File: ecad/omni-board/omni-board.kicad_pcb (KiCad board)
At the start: 2 copper layers, 6 parts, among them J1 Motor_BTS7960_01, J2 Motor_BTS7960_02, J3 Motor_BTS7960_03, J4 Motor_BTS7960_04, U1 ESP32-S3-Zero, U2 ESP32-S3-DevKitC

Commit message: update for production
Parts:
- added C1: 0.1uF, Capacitor_SMD:C_1206_3216Metric_Pad1.33x1.80mm_HandSolder, F.Cu at (144.8, 79.4)
- added C2: 1uF, Capacitor_SMD:CP_Elec_5x5.4, F.Cu at (149.9, 79.4)
- added C3: 22uF, Capacitor_SMD:CP_Elec_5x5.4, F.Cu at (139.1, 92.2)
- added D1: SS14, Diode_SMD:D_SMA_Handsoldering, F.Cu at (148.0, 73.7)
- added D2: LED_Small, LED_SMD:LED_1206_3216Metric_Pad1.42x1.75mm_HandSolder, F.Cu at (128.3, 106.7)
- added D3: LED_Small, LED_SMD:LED_1206_3216Metric_Pad1.42x1.75mm_HandSolder, F.Cu at (128.3, 100.3)
- added D4: LED_Small, LED_SMD:LED_1206_3216Metric_Pad1.42x1.75mm_HandSolder, F.Cu at (128.3, 103.5)
- added H1: MountingHole_Pad, MountingHole:MountingHole_3.2mm_M3_Pad_Via, F.Cu at (180.0, 75.0)
- added H2: MountingHole_Pad, MountingHole:MountingHole_3.2mm_M3_Pad_Via, F.Cu at (130.0, 125.0)
- added H3: MountingHole_Pad, MountingHole:MountingHole_3.2mm_M3_Pad_Via, F.Cu at (180.0, 125.0)
- added H4: MountingHole_Pad, MountingHole:MountingHole_3.2mm_M3_Pad_Via, F.Cu at (130.0, 75.0)
- added J18: Conn_01x04, Connector_Molex:Molex_KK-254_AE-6410-04A_1x04_P2.54mm_Vertical, F.Cu at (181.0, 100.3)
- added J19: Conn_01x04, Connector_Molex:Molex_KK-254_AE-6410-04A_1x04_P2.54mm_Vertical, F.Cu at (181.0, 88.9)
- added J7: Con Batt, Connector_AMASS:AMASS_XT60-M_1x02_P7.20mm_Vertical, F.Cu at (130.2, 92.3)
- added JP1: SolderJumper_3_Open, Jumper:SolderJumper-3_P2.0mm_Open_TrianglePad1.0x1.5mm, F.Cu at (154.9, 108.6)
- added R1: 10k, Resistor_SMD:R_1206_3216Metric_Pad1.30x1.75mm_HandSolder, F.Cu at (168.3, 94.0)
- added R18: 10k, Resistor_SMD:R_1206_3216Metric_Pad1.30x1.75mm_HandSolder, B.Cu at (178.4, 92.4)
- added R19: 10k, Resistor_SMD:R_1206_3216Metric_Pad1.30x1.75mm_HandSolder, B.Cu at (175.9, 92.4)
- added R2: 1k, Resistor_SMD:R_1206_3216Metric_Pad1.30x1.75mm_HandSolder, F.Cu at (134.0, 100.3)
- added R21: 1k, Resistor_SMD:R_1206_3216Metric_Pad1.30x1.75mm_HandSolder, F.Cu at (134.0, 106.7)
- added R22: 1k, Resistor_SMD:R_1206_3216Metric_Pad1.30x1.75mm_HandSolder, F.Cu at (134.0, 103.5)
- U2: value ESP32-S3-DevKitC -> R-78E5.0-1.0; footprint PCM_Espressif:ESP32-S3-DevKitC -> Converter_DCDC:Converter_DCDC_RECOM_R-78E-0.5_THT
- moved J4 41.0 mm to (170.1, 116.2)
- moved J3 40.8 mm to (159.3, 116.2)
- moved J2 40.7 mm to (148.5, 116.2)
- moved J1 40.6 mm to (137.7, 116.2)
- moved U2 37.9 mm to (145.7, 88.4), turned to -90 degrees
- moved U1 28.1 mm to (165.0, 83.8)
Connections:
- U1 pad 1: unconnected-(U1-5V-Pad1) -> Net-(D1-K)
- U1 pad 10: L_PWM_03 -> EN_MOTORS
- U1 pad 13: R_PWM_04 -> L_PWM_04
- U1 pad 14: L_PWM_04 -> R_PWM_04
- U1 pad 15: EN_MOTORS -> L_PWM_03
- U2 pad 1: Net-(U2-3V3-Pad1) -> +12V
- U2 pad 2: Net-(U2-3V3-Pad1) -> GND
- U2 pad 3: unconnected-(U2-CHIP_PU-Pad3) -> +5V
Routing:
- net +3.3V: track 0.00 -> 120.4 mm, vias 0 -> 2
- net EN_MOTORS: track 0.00 -> 67.7 mm
- net +5V: track 0.00 -> 66.9 mm
- net VCC: track 0.00 -> 62.1 mm
- net R_PWM_01: track 0.00 -> 48.2 mm
- net L_PWM_01: track 0.00 -> 43.2 mm
- net L_PWM_03: track 0.00 -> 43.1 mm
- net R_PWM_04: track 0.00 -> 36.4 mm
- net L_PWM_04: track 0.00 -> 33.4 mm
- net +12V: track 0.00 -> 33.1 mm
- net R_PWM_02: track 0.00 -> 32.4 mm
- net SCL: track 0.00 -> 30.3 mm
- net L_PWM_02: track 0.00 -> 28.5 mm
- net R_PWM_03: track 0.00 -> 25.9 mm
- net SDA: track 0.00 -> 24.7 mm
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- added copper zone on B.Cu, net GND
- added copper zone on F.Cu, net GND
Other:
- board outline added: 60 x 60 mm

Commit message: sbus connector added
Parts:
- added J5: Conn_01x03, Connector_PinHeader_2.54mm:PinHeader_1x03_P2.54mm_Vertical, F.Cu at (176.5, 83.2)
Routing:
- net +5V: track 66.9 -> 127.7 mm
- net SBUS: track 0.00 -> 8.95 mm

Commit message: update silkscreen
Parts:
- moved U2 0.97 mm to (144.8, 88.4)
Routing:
- net +5V: track 127.7 -> 130.0 mm
- net +12V: track 33.1 -> 32.2 mm
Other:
- board text added: "+"
- board text added: "12V"
- board text added: "3.3V"
- board text added: "5V"
- board text added: "ESP32-S3 ZERO"
- board text added: "I2C"
- board text added: "MOTOR 1"
- board text added: "MOTOR 2"
- board text added: "MOTOR 3"
- board text added: "MOTOR 4"
- board text added: "Sbus"

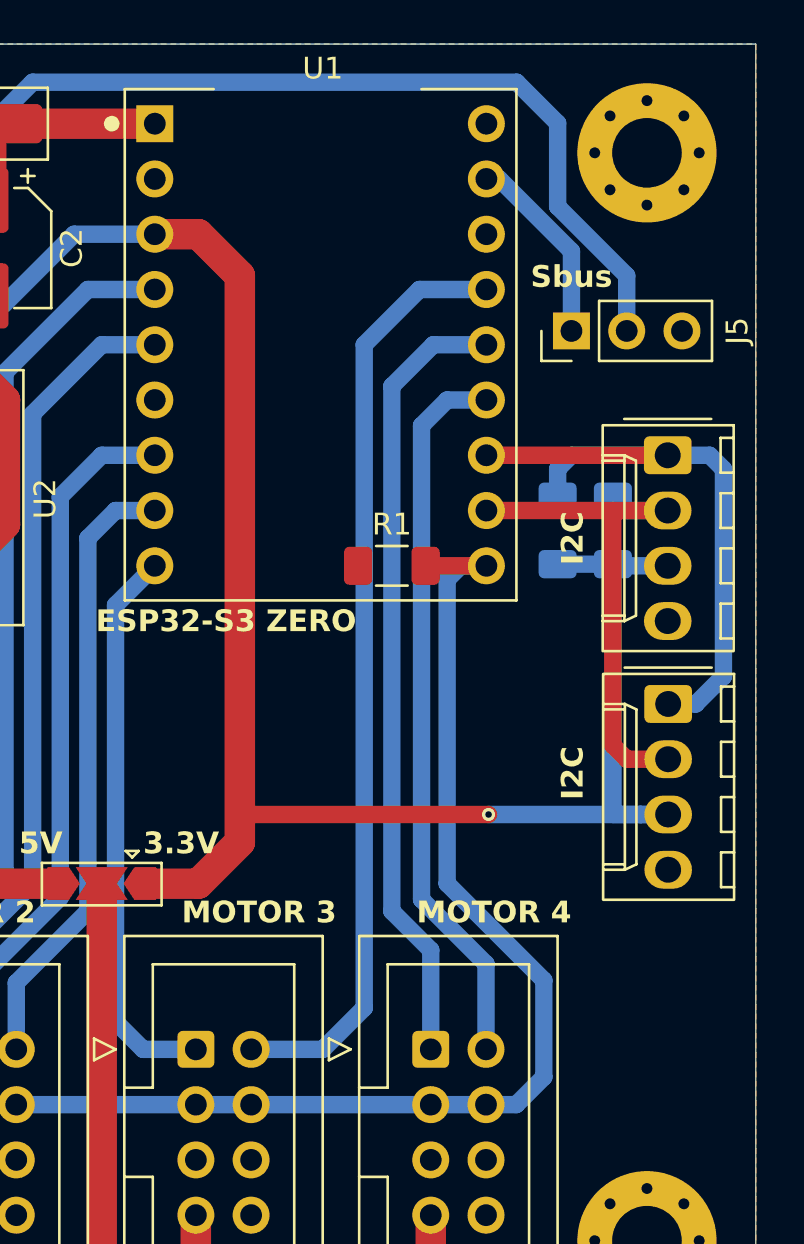
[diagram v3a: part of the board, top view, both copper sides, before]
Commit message: add I2C connector
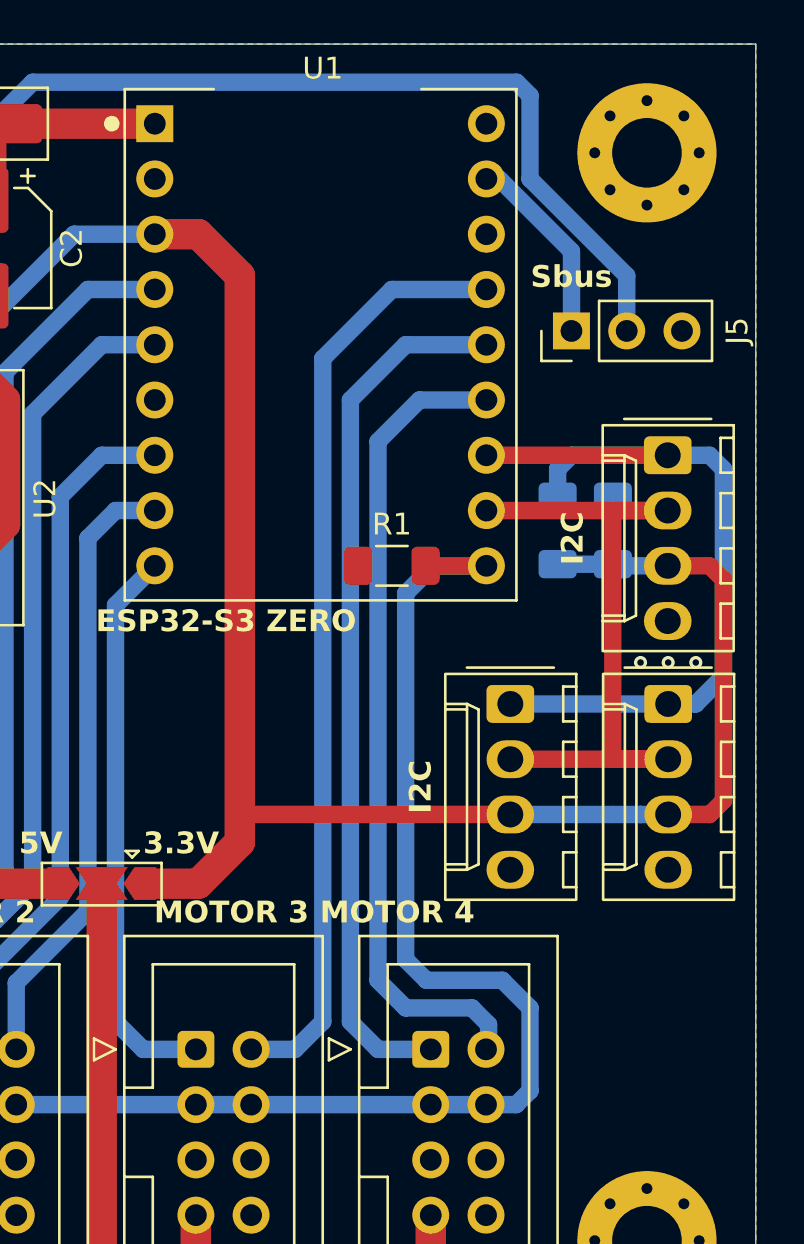
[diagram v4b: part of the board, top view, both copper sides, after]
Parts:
- added J20: Conn_01x04, Connector_Molex:Molex_KK-254_AE-6410-04A_1x04_P2.54mm_Vertical, F.Cu at (173.7, 100.3)
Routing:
- net SDA: track 24.7 -> 32.3 mm
- net SCL: track 30.3 -> 37.6 mm
- net L_PWM_04: track 33.4 -> 37.7 mm
- net EN_MOTORS: track 67.7 -> 71.5 mm
- net R_PWM_04: track 36.4 -> 40.1 mm
- net +3.3V: track 120.4 -> 122.1 mm, vias 2 -> 1
- net GND: vias 0 -> 3
